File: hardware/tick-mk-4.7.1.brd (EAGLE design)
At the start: 96 x 54 mm, 41 parts, among them IC1 TINY85-20-DIP, IC2 DS1307, IC3 L7805, IC4 MAX7219, IC5 MAX7219, J1 PROG, Y2 32.768kHz

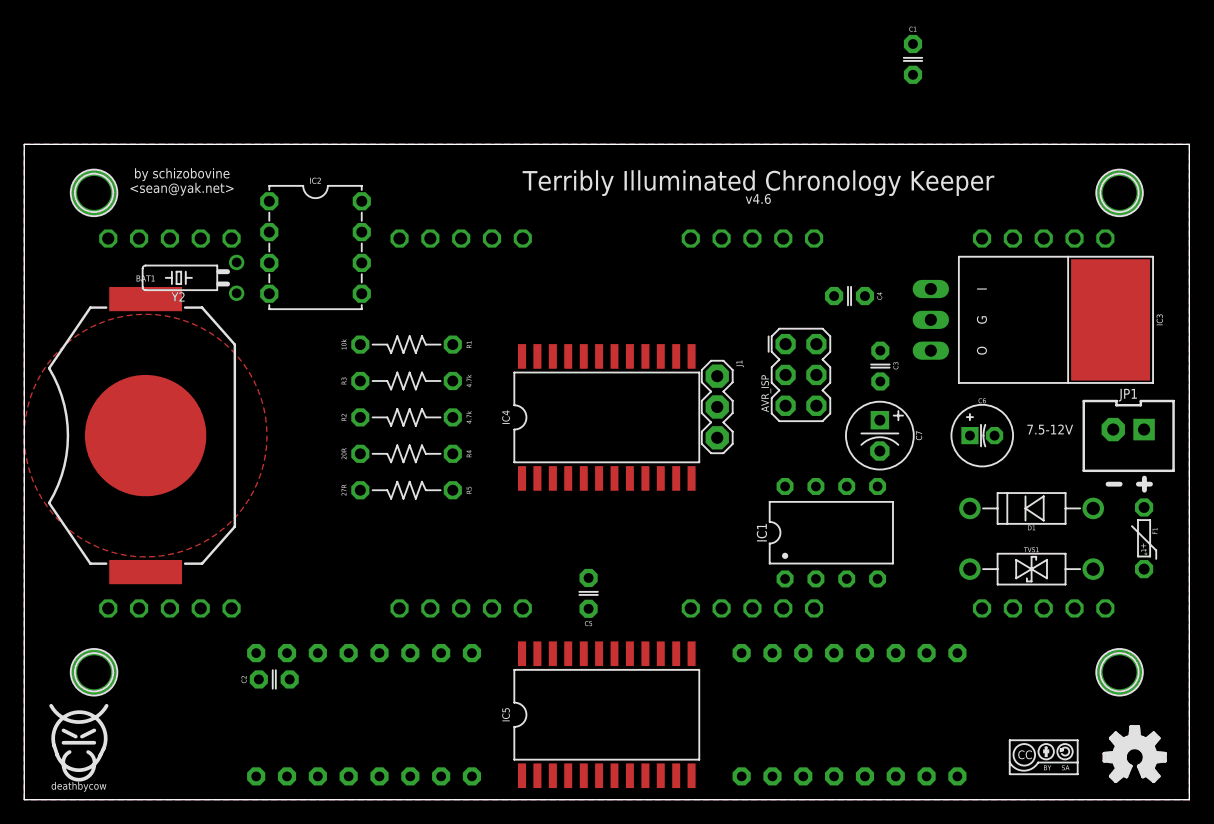
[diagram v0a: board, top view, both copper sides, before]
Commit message: more layout tinkering for the max7129 soic version. broke out into a board with only the two display drivers on it for now, will add other componets once this layout part is done.
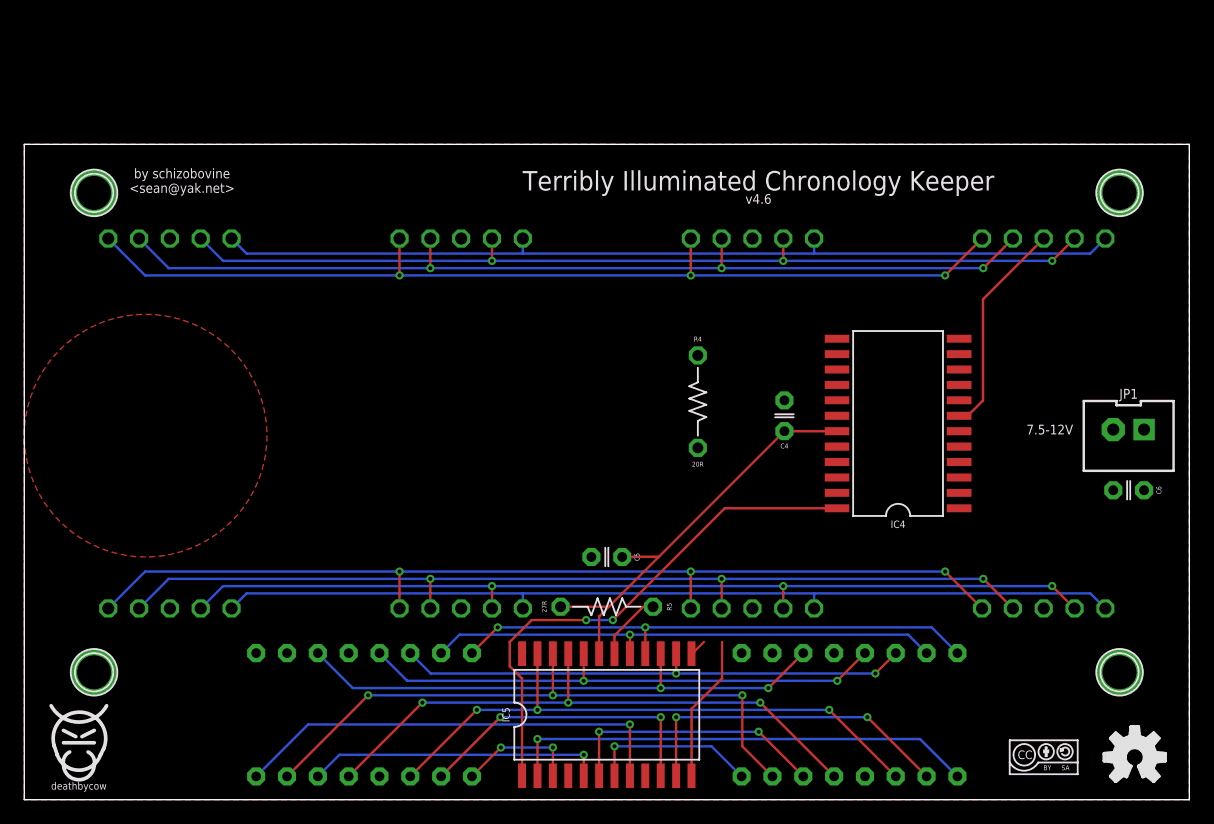
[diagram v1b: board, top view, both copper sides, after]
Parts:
- removed AVR_ISP: AVR_SPI_PRG_6PTH, A_butts:2X3
- removed BAT1: 20mm coincell, A_butts:BATTCON_20MM_MINE
- removed C1, C2, C3: 0.1uF, A_butts:C025-024X044
- removed C7: 100uF, A_butts:E2,5-6
- removed D1: 1N5819, A_butts:DIODE-10.16MM
- removed F1: 500mA, A_butts:PTC-PTH-5.08MM
- removed IC1: TINY85-20-DIP, A_butts:DIP08
- removed IC2: DS1307, A_butts:DIL08
- removed IC3: L7805, A_butts:TO220-IGO-THERMPAD
- removed J1: PROG, A_butts:1X03
- removed R1: 10k, A_butts:RESISTOR-AXIAL-PTH-7.62MM
- removed R2, R3: 4.7k, A_butts:RESISTOR-AXIAL-PTH-7.62MM
- removed TVS1: 5.6V, A_butts:DO-41-TVS-BI-10.16MM
- removed Y2: 32.768kHz, A_butts:TC26H
- C5: value 1uF -> 0.1uF
- C6: value 10uF -> 1uF; device A_butts:E2-5 -> A_butts:C025-024X044
- moved R4 24.4 mm to (55.5, 32.8), turned to 270 degrees
- moved IC4 24.0 mm to (72.0, 31.0), turned to 90 degrees
- moved R5 19.1 mm to (48.0, 15.9)
- moved C6 12.9 mm to (91.0, 25.5), turned to 180 degrees
- moved C4 11.2 mm to (62.6, 31.6), turned to 90 degrees
- moved C5 3.35 mm to (48.0, 20.0), turned to 180 degrees
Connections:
- net N$9 renamed DOUT
- removed net MISO: AVR_ISP.1, J1.1
- removed net MISO/DIN: IC1.6, J1.2
- removed net MOSI/SDA: AVR_ISP.4, IC1.5, IC2.6, R2.P$2
- removed net N$1: BAT1.TOP@1, BAT1.TOP@2, IC2.3
- removed net N$2: IC2.1, Y2.2
- removed net N$3: IC2.2, Y2.1
- removed net N$4: D1.A, F1.P$2, TVS1.P$2
- removed net N$7: F1.P$1, JP1.1
- removed net N$8: C6.+, D1.C, IC3.IN
- removed net RST: AVR_ISP.5, IC1.1, R1.P$1
- removed net SCK/SCL: AVR_ISP.3, IC1.7, IC2.5, R3.P$2
- net CLK: no longer IC1.2
- net DIN: no longer J1.3
- net GND: now also C6.2; no longer AVR_ISP.6, BAT1.BOTTOM, C1.2, C2.2, C3.2, C6.-, C7.-, IC1.4, IC2.4, IC3.4, IC3.GND, TVS1.P$1
- net LOAD: no longer IC1.3
- net VCC: now also C6.1, JP1.1; no longer AVR_ISP.2, C1.1, C2.1, C3.1, C7.+, IC1.8, IC2.8, IC3.OUT, R1.P$2, R2.P$1, R3.P$1
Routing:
- net DP2: track 0.00 -> 80.6 mm, vias 0 -> 3
- net B2: track 0.00 -> 80.6 mm, vias 0 -> 3
- net A2: track 0.00 -> 78.9 mm, vias 0 -> 3
- net C2: track 0.00 -> 78.9 mm, vias 0 -> 3
- net F2: track 0.00 -> 77.2 mm, vias 0 -> 3
- net D2: track 0.00 -> 77.2 mm, vias 0 -> 3
- net G2: track 0.00 -> 75.5 mm
- net E2: track 0.00 -> 75.5 mm
- net DP1: track 0.00 -> 51.4 mm, vias 0 -> 3
- net D1: track 0.00 -> 49.2 mm, vias 0 -> 3
- net E1: track 0.00 -> 49.1 mm, vias 0 -> 3
- net F1: track 0.00 -> 45.2 mm, vias 0 -> 2
- net C1: track 0.00 -> 44.1 mm, vias 0 -> 2
- net B1: track 0.00 -> 43.9 mm, vias 0 -> 2
- net A1: track 0.00 -> 43.0 mm, vias 0 -> 2
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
